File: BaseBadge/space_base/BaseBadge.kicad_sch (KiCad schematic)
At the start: 7 parts, among them J1 Conn_02x03_Counter_Clockwise, J2 Conn_02x03_Counter_Clockwise, J3 Conn_02x03_Counter_Clockwise, J4 Conn_02x03_Counter_Clockwise, J5 Conn_02x03_Counter_Clockwise, SW1 SW_SPDT

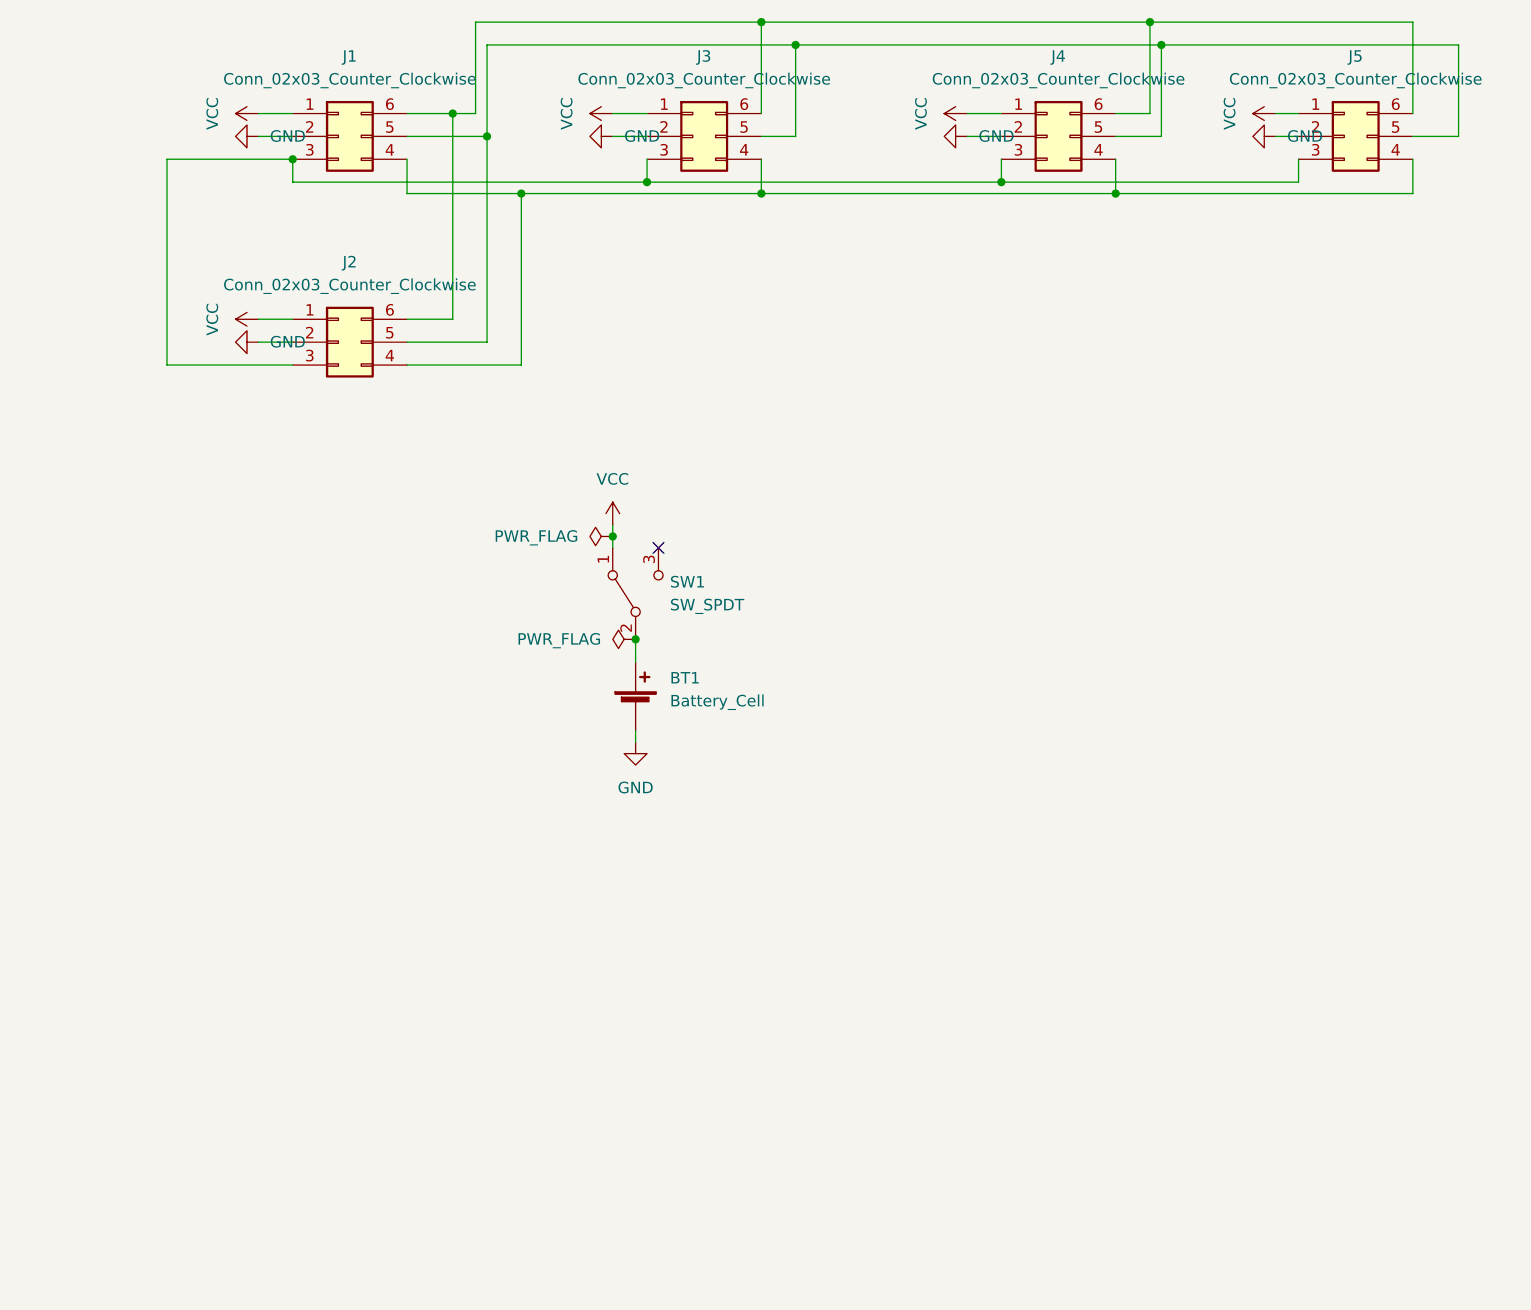
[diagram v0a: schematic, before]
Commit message: overhauls across boards to v02
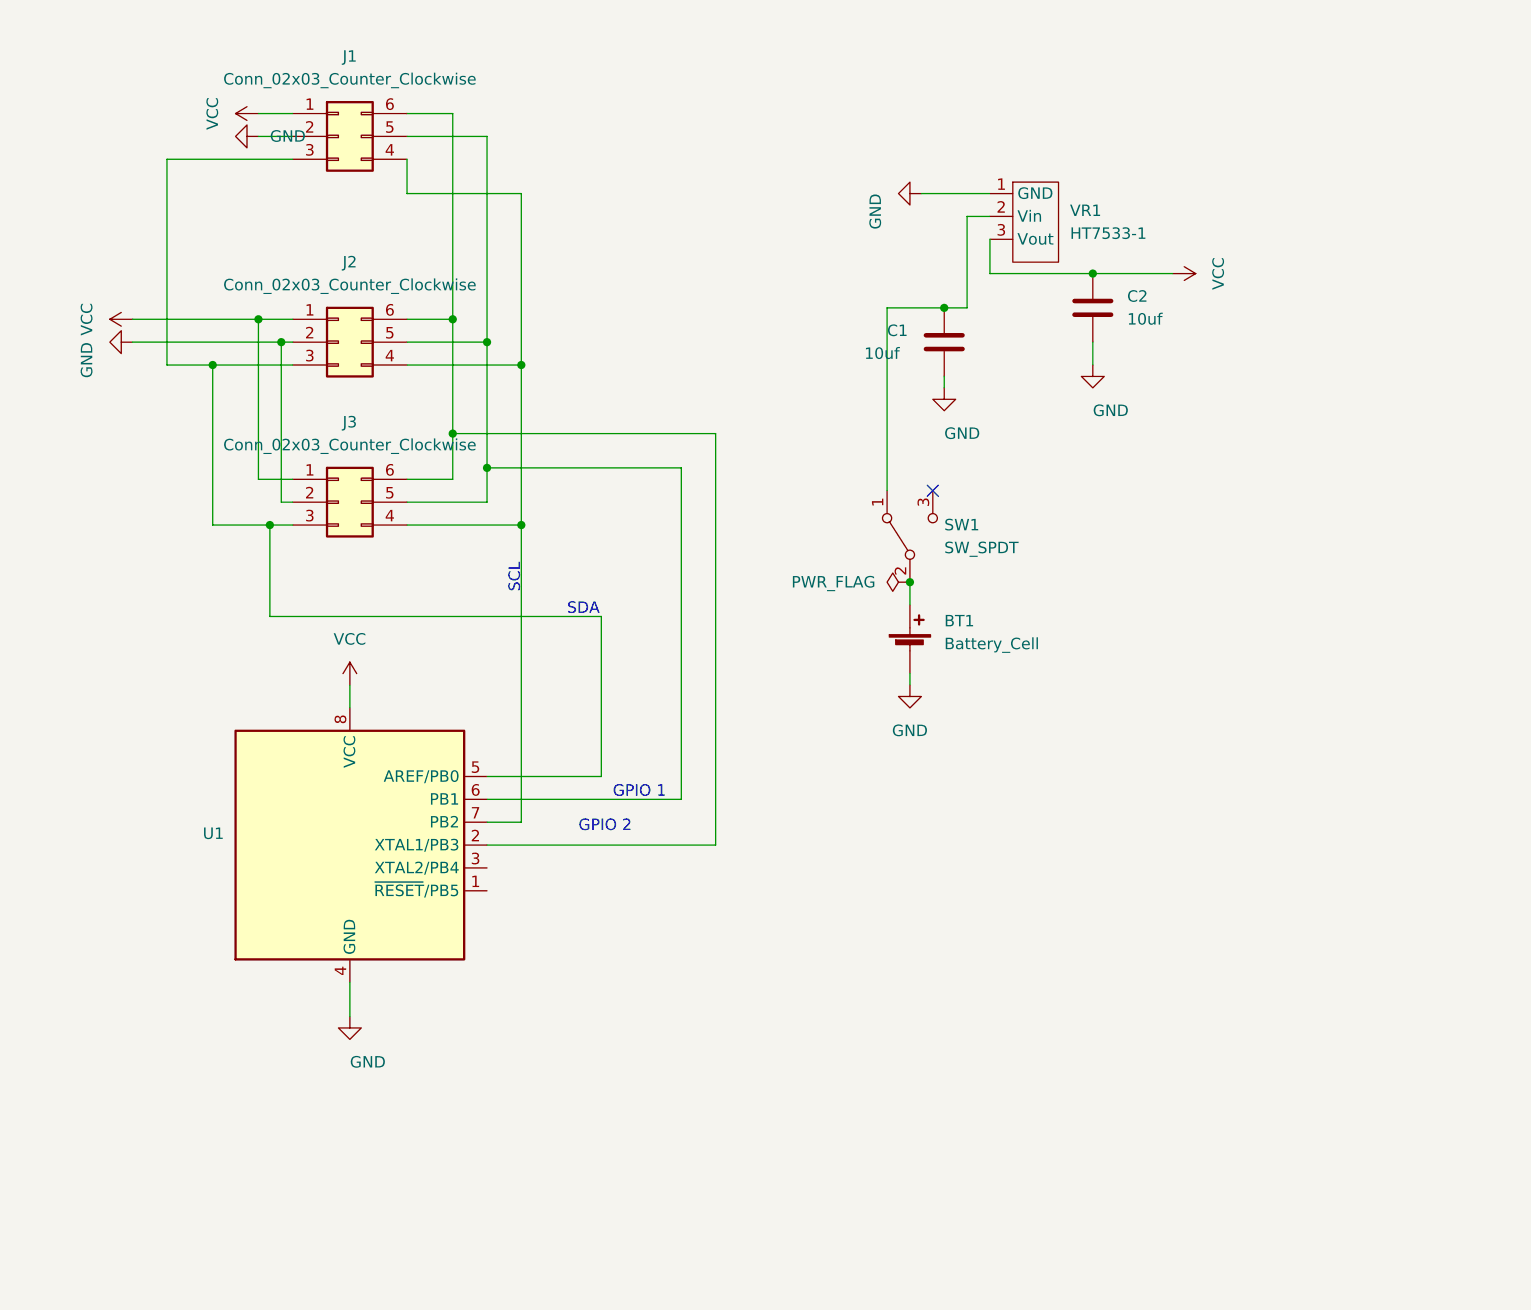
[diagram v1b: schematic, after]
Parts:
- removed J4, J5: Conn_02x03_Counter_Clockwise, Connector_PinSocket_2.54mm:PinSocket_2x03_P2.54mm_Vertical, symbol Connector_Generic:Conn_02x03_Counter_Clockwise
- added C1, C2: 10uf, Capacitor_SMD:C_0805_2012Metric, symbol Device:C
- added U1: (no value), symbol MCU_Microchip_ATtiny:ATtiny85-20S
- added VR1: HT7533-1, Package_TO_SOT_SMD:SOT-89-3, symbol avBadge_2022:HT7533-1
- J1: footprint (none) -> SpaceBase_Library:space2sky_connector
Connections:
- net GND: now also C1.2, C2.2, U1.4 (GND), VR1.1 (GND)
- net VCC: now also C2.1, U1.8 (VCC), VR1.3 (Vout); no longer SW1.1 (A)
- net at J1.3 (Pin_3), J2.3 (Pin_3), J3.3 (Pin_3): now also U1.5 (AREF/PB0)
- net at J1.4 (Pin_4), J2.4 (Pin_4), J3.4 (Pin_4): now also U1.7 (PB2)
- net at J1.5 (Pin_5), J2.5 (Pin_5), J3.5 (Pin_5): now also U1.6 (PB1)
- net at J1.6 (Pin_6), J2.6 (Pin_6), J3.6 (Pin_6): now also U1.2 (XTAL1/PB3)
- new net: C1.1, SW1.1 (A), VR1.2 (Vin)
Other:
- note added: "GPIO 1"
- note added: "GPIO 2"
- note added: "SCL"
- note added: "SDA"
- moved on the sheet: BT1, SW1

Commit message: added artwork to back of base badge
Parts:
- added R1, R2: (no value), symbol Device:R
- U1: value (none) -> ATtiny85-20S; footprint (none) -> Package_SO:SOIC-8W_5.3x5.3mm_P1.27mm
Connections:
- net VCC: now also R1.1, R2.1
- net at J1.3 (Pin_3), J2.3 (Pin_3), J3.3 (Pin_3)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: now also R2.2
- net at J1.4 (Pin_4), J2.4 (Pin_4), J3.4 (Pin_4)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: now also R1.2
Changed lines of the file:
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@@
   (junction (at 76.2 104.14) (diameter 0) (color 0 0 0 0)
   )
+  (junction (at 76.2 111.76) (diameter 0) (color 0 0 0 0)
+  )
   (junction (at 48.26 104.14) (diameter 0) (color 0 0 0 0)
   )
@@
   )
   (junction (at 119.38 110.49) (diameter 0) (color 0 0 0 0)
+  )
+  (junction (at 52.07 114.3) (diameter 0) (color 0 0 0 0)
   )
   (junction (at 46.99 81.28) (diameter 0) (color 0 0 0 0)
@@
     (stroke (width 0) (type default) (color 0 0 0 0))
   )
+  (wire (pts (xy 52.07 114.3) (xy 48.26 114.3))
+    (stroke (width 0) (type default) (color 0 0 0 0))
+  )
   (wire (pts (xy 76.2 86.36) (xy 76.2 104.14))
     (stroke (width 0) (type default) (color 0 0 0 0))
@@
     (stroke (width 0) (type default) (color 0 0 0 0))
   )
+  (wire (pts (xy 26.67 111.76) (xy 29.21 111.76))
+    (stroke (width 0) (type default) (color 0 0 0 0))
+  )
   (wire (pts (xy 46.99 99.06) (xy 50.8 99.06))
     (stroke (width 0) (type default) (color 0 0 0 0))
@@
     (stroke (width 0) (type default) (color 0 0 0 0))
   )
-  (wire (pts (xy 76.2 137.16) (xy 76.2 104.14))
+  (wire (pts (xy 76.2 137.16) (xy 76.2 111.76))
     (stroke (width 0) (type default) (color 0 0 0 0))
   )
@@
     (stroke (width 0) (type default) (color 0 0 0 0))
   )
+  (wire (pts (xy 26.67 120.65) (xy 29.21 120.65))
+    (stroke (width 0) (type default) (color 0 0 0 0))
+  )
   (wire (pts (xy 93.98 97.79) (xy 72.39 97.79))
     (stroke (width 0) (type default) (color 0 0 0 0))
   )
+  (wire (pts (xy 52.07 120.65) (xy 52.07 114.3))
+    (stroke (width 0) (type default) (color 0 0 0 0))
+  )
   (wire (pts (xy 76.2 67.31) (xy 76.2 86.36))
     (stroke (width 0) (type default) (color 0 0 0 0))
@@
     (stroke (width 0) (type default) (color 0 0 0 0))
   )
+  (wire (pts (xy 36.83 120.65) (xy 52.07 120.65))
+    (stroke (width 0) (type default) (color 0 0 0 0))
+  )
+  (wire (pts (xy 76.2 111.76) (xy 76.2 104.14))
+    (stroke (width 0) (type default) (color 0 0 0 0))
+  )
   (wire (pts (xy 63.5 58.42) (xy 68.58 58.42))
     (stroke (width 0) (type default) (color 0 0 0 0))
@@
     (stroke (width 0) (type default) (color 0 0 0 0))
   )
-  (wire (pts (xy 85.09 114.3) (xy 48.26 114.3))
+  (wire (pts (xy 85.09 114.3) (xy 52.07 114.3))
     (stroke (width 0) (type default) (color 0 0 0 0))
   )
@@
   )
   (wire (pts (xy 46.99 58.42) (xy 50.8 58.42))
+    (stroke (width 0) (type default) (color 0 0 0 0))
+  )
+  (wire (pts (xy 36.83 111.76) (xy 76.2 111.76))
     (stroke (width 0) (type default) (color 0 0 0 0))
   )
@@
   (text "GPIO 1" (at 86.36 134.62 0)
     (effects (font (size 1.27 1.27)) (justify left bottom))
+  )
+  (symbol (lib_id "power:VCC") (at 26.67 111.76 90) (unit 1)
+    (in_bom yes) (on_board yes)
+    (property "Reference" "#PWR01" (id 0) (at 30.48 111.76 0)
+      (effects (font (size 1.27 1.27)) hide)
+    )
+    (property "Value" "VCC" (id 1) (at 21.59 111.76 0))
+    (property "Footprint" "" (id 2) (at 26.67 111.76 0)
+      (effects (font (size 1.27 1.27)) hide)
+    )
+    (property "Datasheet" "" (id 3) (at 26.67 111.76 0)
+      (effects (font (size 1.27 1.27)) hide)
+    )
+    (pin "1")
   )
   (symbol (lib_id "power:GND") (at 119.38 121.92 0) (unit 1)
@@
     (pin "6")
   )
+  (symbol (lib_id "power:VCC") (at 26.67 120.65 90) (unit 1)
+    (in_bom yes) (on_board yes)
+    (property "Reference" "#PWR02" (id 0) (at 30.48 120.65 0)
+      (effects (font (size 1.27 1.27)) hide)
+    )
+    (property "Value" "VCC" (id 1) (at 21.59 120.65 0))
+    (property "Footprint" "" (id 2) (at 26.67 120.65 0)
+      (effects (font (size 1.27 1.27)) hide)
+    )
+    (property "Datasheet" "" (id 3) (at 26.67 120.65 0)
+      (effects (font (size 1.27 1.27)) hide)
+    )
+    (pin "1")
+  )
+  (symbol (lib_id "Device:R") (at 33.02 111.76 90) (unit 1)
+    (in_bom yes) (on_board yes) (fields_autoplaced)
+    (property "Reference" "R1" (id 0) (at 33.02 105.41 90))
+    (property "Value" "" (id 1) (at 33.02 107.95 90))
+    (property "Footprint" "" (id 2) (at 33.02 113.538 90)
+      (effects (font (size 1.27 1.27)) hide)
+    )
+    (property "Datasheet" "~" (id 3) (at 33.02 111.76 0)
+      (effects (font (size 1.27 1.27)) hide)
+    )
+    (pin "1")
+    (pin "2")
+  )
   (symbol (lib_id "power:VCC") (at 148.59 76.2 270) (unit 1)
     (in_bom yes) (on_board yes)
@@
     (pin "6")
   )
+  (symbol (lib_id "Device:R") (at 33.02 120.65 90) (unit 1)
+    (in_bom yes) (on_board yes) (fields_autoplaced)
+    (property "Reference" "R2" (id 0) (at 33.02 114.3 90))
+    (property "Value" "" (id 1) (at 33.02 116.84 90))
+    (property "Footprint" "" (id 2) (at 33.02 122.428 90)
+      (effects (font (size 1.27 1.27)) hide)
+    )
+    (property "Datasheet" "~" (id 3) (at 33.02 120.65 0)
+      (effects (font (size 1.27 1.27)) hide)
+    )
+    (pin "1")
+    (pin "2")
+  )
   (symbol (lib_id "MCU_Microchip_ATtiny:ATtiny85-20S") (at 57.15 139.7 0) (unit 1)
     (in_bom yes) (on_board yes) (fields_autoplaced)
@@
       (effects (font (size 1.27 1.27)) (justify right))
     )
-    (property "Value" "" (id 1) (at 43.18 140.9699 0)
+    (property "Value" "ATtiny85-20S" (id 1) (at 43.18 140.9699 0)
       (effects (font (size 1.27 1.27)) (justify right))
     )
-    (property "Footprint" "" (id 2) (at 57.15 139.7 0)
+    (property "Footprint" "Package_SO:SOIC-8W_5.3x5.3mm_P1.27mm" (id 2) (at 57.15 139.7 0)
       (effects (font (size 1.27 1.27) italic) hide)
     )
@@
       (reference "#FLG0101") (unit 1) (value "PWR_FLAG") (footprint "")
     )
+    (path "/04814e1b-c013-4fd0-9fc5-f898fc8ddbab"
+      (reference "#PWR01") (unit 1) (value "VCC") (footprint "")
+    )
+    (path "/79b750e2-d681-4be1-803e-075bb9e2416c"
+      (reference "#PWR02") (unit 1) (value "VCC") (footprint "")
+    )
     (path "/83c94693-d97b-4657-80e6-a20a4bc00865"
       (reference "#PWR0101") (unit 1) (value "VCC") (footprint "")
@@
       (reference "J3") (unit 1) (value "Conn_02x03_Counter_Clockwise") (footprint "Connector_PinSocket_2.54mm:PinSocket_2x03_P2.54mm_Vertical")
     )
+    (path "/7aec2799-4000-4098-a752-1bed4b75fdcf"
+      (reference "R1") (unit 1) (value "4.7K") (footprint "Resistor_SMD:R_0805_2012Metric")
+    )
+    (path "/dea17859-4b35-4115-a09c-975f56c2272b"
+      (reference "R2") (unit 1) (value "4.7K") (footprint "Resistor_SMD:R_0805_2012Metric")
+    )
     (path "/bbeb4758-2d88-449c-a139-6d130c88e4f6"

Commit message: updated base badge, shuttle, and warning
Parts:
- added J4: (no value), symbol Connector:AVR-ISP-6
- R1, R2: value (none) -> 4.7K; footprint (none) -> Resistor_SMD:R_0805_2012Metric
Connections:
- net GND: now also J4.6 (GND)
- net VCC: now also J4.2 (VCC)
- net at J1.3 (Pin_3), J2.3 (Pin_3), J3.3 (Pin_3)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: now also J4.4 (MOSI)
- net at J1.4 (Pin_4), J2.4 (Pin_4), J3.4 (Pin_4)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: now also J4.3 (SCK)
- net at J1.5 (Pin_5), J2.5 (Pin_5), J3.5 (Pin_5)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: now also J4.1 (MISO)
- net at U1.1 (~{RESET}/PB5): now also J4.5 (~{RST})

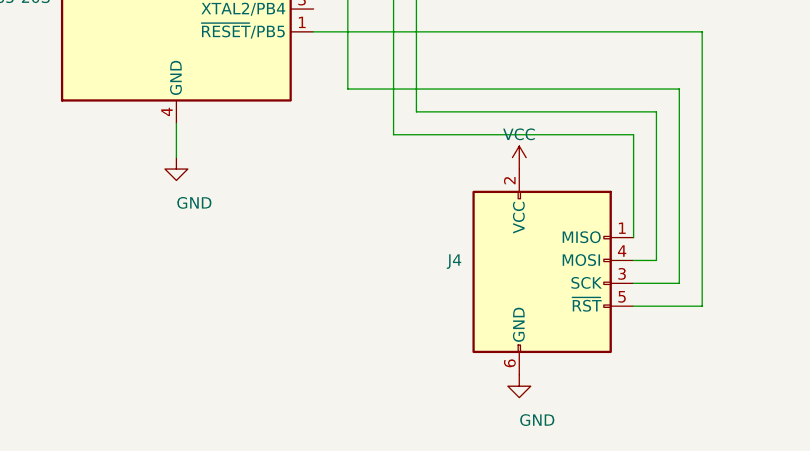
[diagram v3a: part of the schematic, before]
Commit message: v04 of base badge and arduino addition.
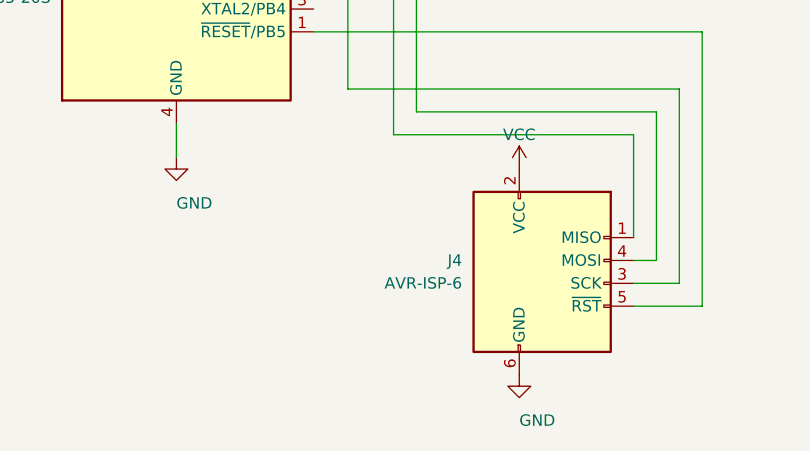
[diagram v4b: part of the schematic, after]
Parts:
- J4: value (none) -> AVR-ISP-6; footprint (none) -> aerospace_badge:AVR-ISP-6
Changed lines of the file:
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@@
       (effects (font (size 1.27 1.27)) (justify right))
     )
-    (property "Value" "" (id 1) (at 88.9 172.7199 0)
+    (property "Value" "AVR-ISP-6" (id 1) (at 88.9 172.7199 0)
       (effects (font (size 1.27 1.27)) (justify right))
     )
-    (property "Footprint" "" (id 2) (at 91.44 171.45 90)
+    (property "Footprint" "aerospace_badge:AVR-ISP-6" (id 2) (at 91.44 171.45 90)
       (effects (font (size 1.27 1.27)) hide)
     )
